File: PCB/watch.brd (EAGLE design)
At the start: 81.1 x 53.1 mm, 58 parts, among them IC1 ISL1209, J2 USB-MICROB, Q1 32.768 KHz, T1 BC850, U2 MKL27Z256VLH4

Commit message: wired more of the SR
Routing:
- net PTB18: track 0.00 -> 54.9 mm, vias 0 -> 1
- net PTC0: track 0.00 -> 47.3 mm, vias 0 -> 1
- net N$28: track 0.00 -> 47.1 mm
- net PTC7: track 0.00 -> 42.4 mm, vias 0 -> 1
- net PTB17: track 0.00 -> 35.7 mm, vias 0 -> 1
- net N$21: track 18.4 -> 26.9 mm, vias 1 -> 2
- net V+: track 0.00 -> 3.90 mm, vias 0 -> 2
- net GND: track 0.00 -> 2.75 mm, vias 0 -> 1
- net N$47: track 45.5 -> 44.9 mm

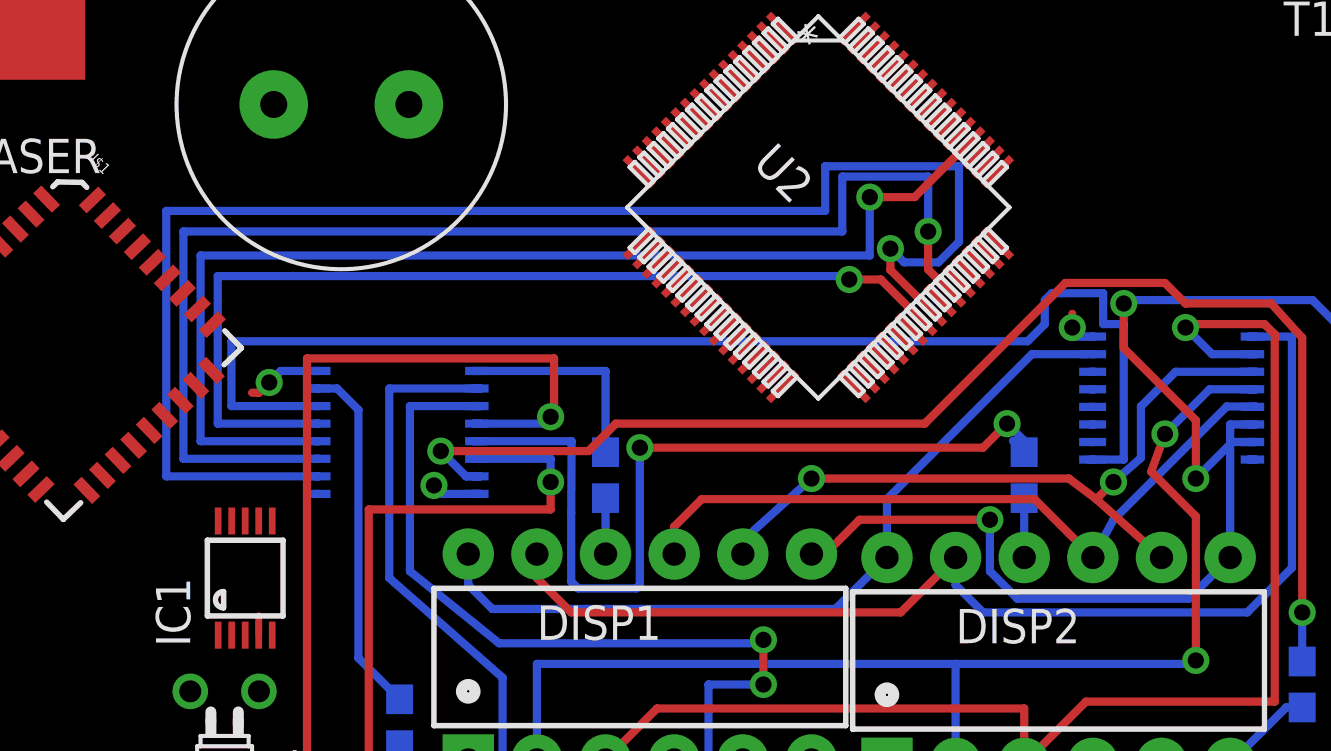
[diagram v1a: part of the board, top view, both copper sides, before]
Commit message: wired all SR but one pin
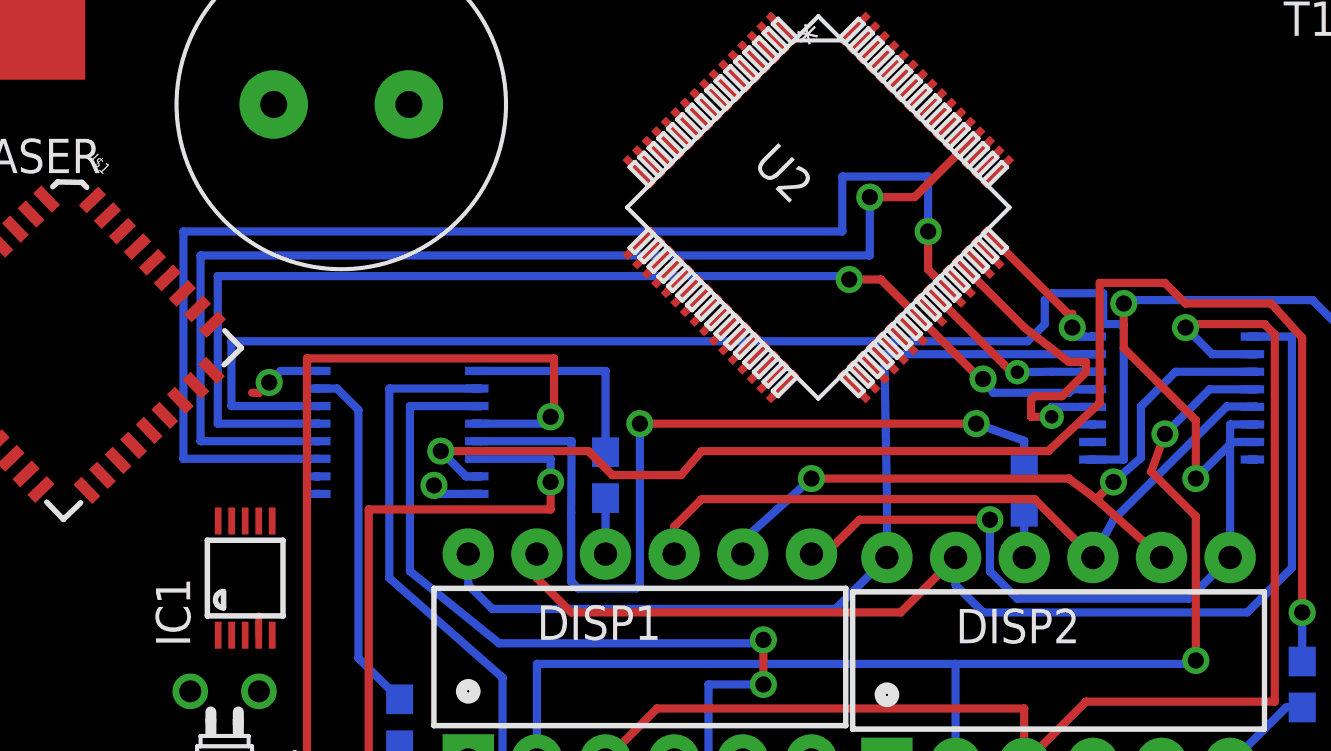
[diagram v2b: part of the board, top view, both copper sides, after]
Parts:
- moved R8 0.51 mm to (58.3, 31.5)
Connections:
- net PTB18: no longer U$4.MR, U$5.MR
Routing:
- net PTB18: track 54.9 -> 0.00 mm, vias 1 -> 0
- net PTC2: track 0.00 -> 11.5 mm, vias 0 -> 1
- net PTB17: track 35.7 -> 43.1 mm, vias 1 -> 2
- net PTB19: track 0.00 -> 6.54 mm, vias 0 -> 1
- net V+: track 3.90 -> 7.75 mm
- net N$29: track 49.2 -> 52.5 mm
- net N$11: track 29.6 -> 32.8 mm
- net N$15: track 2.20 -> 1.69 mm
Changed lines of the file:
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@@
 <element name="R6" library="SparkFun-Resistors" package="0603-RES" value="680" x="42.545" y="19.177" rot="MR0"/>
 <element name="R7" library="SparkFun-Resistors" package="0603-RES" value="680" x="51.689" y="19.304" rot="MR0"/>
-<element name="R8" library="SparkFun-Resistors" package="0603-RES" value="680" x="58.293" y="32.004" rot="MR90"/>
+<element name="R8" library="SparkFun-Resistors" package="0603-RES" value="680" x="58.293" y="31.496" rot="MR90"/>
 <element name="R9" library="SparkFun-Resistors" package="0603-RES" value="680" x="60.198" y="18.669" rot="MR0"/>
 <element name="S1" library="adafruit" package="EG1213" value="EG1213" x="79.248" y="57.785" rot="R180"/>
@@
 <via x="60.071" y="37.465" extent="1-16" drill="0.6" shape="square"/>
 <wire x1="60.071" y1="37.465" x2="60.071" y2="37.973" width="0.3048" layer="1"/>
+<wire x1="60.071" y1="37.973" x2="59.91330625" y2="37.973" width="0.3048" layer="1"/>
+<wire x1="59.91330625" y1="37.973" x2="57.302134375" y2="40.584171875" width="0.3048" layer="1"/>
 <wire x1="60.628" y1="37.129" x2="72.51" y2="40.35" width="0" layer="19" extent="1-16"/>
-<wire x1="57.302134375" y1="40.584171875" x2="60.071" y2="37.973" width="0" layer="19" extent="1-1"/>
 <wire x1="48.640065625" y1="35.98796875" x2="57.302134375" y2="40.584171875" width="0" layer="19" extent="1-1"/>
 <wire x1="45.104521875" y1="44.29648125" x2="48.640065625" y2="35.98796875" width="0" layer="19" extent="1-1"/>
@@
 <contactref element="U$5" pad="Q5"/>
 <contactref element="R8" pad="2"/>
-<wire x1="58.293" y1="32.854" x2="57.873" y2="33.274" width="0.3048" layer="16"/>
-<wire x1="44.069" y1="33.02" x2="44.069" y2="27.94" width="0.3048" layer="16"/>
+<wire x1="44.069" y1="33.909" x2="44.069" y2="27.94" width="0.3048" layer="16"/>
 <wire x1="44.069" y1="27.94" x2="43.942" y2="27.813" width="0.3048" layer="16"/>
 <wire x1="43.942" y1="27.813" x2="41.783" y2="27.813" width="0.3048" layer="16"/>
@@
 <wire x1="41.529" y1="30.607" x2="41.544" y2="33.259" width="0.3048" layer="16"/>
 <wire x1="41.544" y1="33.259" x2="38.166" y2="33.259" width="0.3048" layer="16"/>
-<via x="44.069" y="33.02" extent="1-16" drill="0.6" shape="square"/>
-<wire x1="44.069" y1="33.02" x2="56.769" y2="33.02" width="0.3048" layer="1"/>
-<wire x1="56.769" y1="33.02" x2="57.658" y2="33.909" width="0.3048" layer="1"/>
-<via x="57.658" y="33.909" extent="1-16" drill="0.6" shape="square"/>
-<wire x1="57.658" y1="33.909" x2="58.293" y2="33.274" width="0.3048" layer="16"/>
-<wire x1="58.293" y1="33.274" x2="58.293" y2="32.854" width="0.3048" layer="16"/>
+<via x="44.069" y="33.909" extent="1-16" drill="0.6" shape="square"/>
+<wire x1="44.069" y1="33.909" x2="56.515" y2="33.909" width="0.3048" layer="1"/>
+<via x="56.515" y="33.909" extent="1-16" drill="0.6" shape="square"/>
+<wire x1="56.515" y1="33.909" x2="58.293" y2="33.274" width="0.3048" layer="16"/>
+<wire x1="58.293" y1="33.274" x2="58.293" y2="32.346" width="0.3048" layer="16"/>
 </signal>
 <signal name="N$23">
@@
 <via x="36.703" y="32.893" extent="1-16" drill="0.6"/>
 <wire x1="36.703" y1="32.893" x2="42.164" y2="32.893" width="0.3048" layer="1"/>
-<wire x1="42.164" y1="32.893" x2="43.18" y2="33.909" width="0.3048" layer="1"/>
-<wire x1="54.61" y1="33.909" x2="59.817" y2="39.116" width="0.3048" layer="1"/>
-<wire x1="59.817" y1="39.116" x2="63.5" y2="39.116" width="0.3048" layer="1"/>
 <wire x1="63.5" y1="39.116" x2="64.262" y2="38.354" width="0.3048" layer="1"/>
 <wire x1="64.262" y1="38.354" x2="67.437" y2="38.354" width="0.3048" layer="1"/>
@@
 <via x="68.58" y="26.924" extent="1-16" drill="0.6"/>
 <wire x1="68.58" y1="26.924" x2="68.58" y2="25.107" width="0.3048" layer="16"/>
-<wire x1="43.18" y1="33.909" x2="54.61" y2="33.909" width="0.3048" layer="1"/>
+<wire x1="63.5" y1="39.116" x2="61.087" y2="39.116" width="0.3048" layer="1"/>
+<wire x1="61.087" y1="39.116" x2="61.087" y2="34.671" width="0.3048" layer="1"/>
+<wire x1="61.087" y1="34.671" x2="59.182" y2="32.893" width="0.3048" layer="1"/>
+<wire x1="59.182" y1="32.893" x2="46.355" y2="32.893" width="0.3048" layer="1"/>
+<wire x1="46.355" y1="32.893" x2="45.593" y2="32.004" width="0.3048" layer="1"/>
+<wire x1="45.593" y1="32.004" x2="43.053" y2="32.004" width="0.3048" layer="1"/>
+<wire x1="43.053" y1="32.004" x2="42.164" y2="32.893" width="0.3048" layer="1"/>
 </signal>
 <signal name="N$31">
@@
 <wire x1="51.816" y1="39.243" x2="52.986459375" y2="39.243" width="0.3048" layer="1"/>
 <wire x1="52.986459375" y1="39.243" x2="54.473709375" y2="37.75575" width="0.3048" layer="1"/>
-<wire x1="54.473709375" y1="37.75575" x2="60.628" y2="35.179" width="0" layer="19" extent="1-16"/>
+<wire x1="57.15" y1="35.052" x2="56.769" y2="35.56" width="0.3048" layer="16"/>
+<via x="56.769" y="35.56" extent="1-16" drill="0.6" shape="square"/>
+<wire x1="56.769" y1="35.56" x2="56.669459375" y2="35.56" width="0.3048" layer="1"/>
+<wire x1="56.669459375" y1="35.56" x2="54.473709375" y2="37.75575" width="0.3048" layer="1"/>
+<wire x1="57.15" y1="35.052" x2="59.944" y2="35.052" width="0.3048" layer="16"/>
+<wire x1="59.944" y1="35.052" x2="60.071" y2="35.179" width="0.3048" layer="16"/>
+<wire x1="60.071" y1="35.179" x2="60.628" y2="35.179" width="0.3048" layer="16"/>
 </signal>
 <signal name="PTB18">
-<contactref element="U$5" pad="MR"/>
-<contactref element="U$4" pad="MR"/>
 <contactref element="U2" pad="41"/>
-<wire x1="31.926" y1="31.959" x2="26.543" y2="31.959" width="0.3048" layer="16"/>
-<wire x1="26.543" y1="31.959" x2="26.543" y2="41.783" width="0.3048" layer="16"/>
-<wire x1="26.543" y1="41.783" x2="50.927" y2="41.783" width="0.3048" layer="16"/>
-<wire x1="50.927" y1="41.783" x2="50.927" y2="43.434" width="0.3048" layer="16"/>
-<wire x1="50.927" y1="43.434" x2="55.88" y2="43.434" width="0.3048" layer="16"/>
-<wire x1="55.88" y1="43.434" x2="55.88" y2="40.64" width="0.3048" layer="16"/>
-<wire x1="55.88" y1="40.64" x2="55.118" y2="39.878" width="0.3048" layer="16"/>
-<wire x1="55.118" y1="39.878" x2="53.848" y2="39.878" width="0.3048" layer="16"/>
-<wire x1="53.848" y1="39.878" x2="53.34" y2="40.386" width="0.3048" layer="16"/>
-<via x="53.34" y="40.386" extent="1-16" drill="0.6" shape="square"/>
-<wire x1="53.34" y1="40.386" x2="53.34" y2="39.596534375" width="0.3048" layer="1"/>
-<wire x1="53.34" y1="39.596534375" x2="54.827246875" y2="38.1092875" width="0.3048" layer="1"/>
-<wire x1="54.827246875" y1="38.1092875" x2="60.628" y2="33.229" width="0" layer="19" extent="1-16"/>
 </signal>
 <signal name="PTB19">
 <contactref element="U$4" pad="DS"/>
 <contactref element="U2" pad="42"/>
-<wire x1="55.18081875" y1="38.46285625" x2="60.628" y2="35.829" width="0" layer="19" extent="1-16"/>
+<wire x1="60.628" y1="35.829" x2="59.324" y2="35.829" width="0.3048" layer="16"/>
+<wire x1="59.324" y1="35.829" x2="58.039" y2="35.814" width="0.3048" layer="16"/>
+<via x="58.039" y="35.814" extent="1-16" drill="0.5"/>
+<wire x1="58.039" y1="35.814" x2="57.829675" y2="35.814" width="0.3048" layer="1"/>
+<wire x1="57.829675" y1="35.814" x2="55.18081875" y2="38.46285625" width="0.3048" layer="1"/>
 </signal>
 <signal name="PTB1">
@@
 <contactref element="U2" pad="45"/>
 <contactref element="U$4" pad="STCP"/>
-<wire x1="60.628" y1="34.529" x2="56.241475" y2="39.523515625" width="0" layer="19" extent="1-16"/>
+<wire x1="60.628" y1="34.529" x2="59.309" y2="34.529" width="0.3048" layer="16"/>
+<wire x1="59.309" y1="34.529" x2="59.309" y2="34.163" width="0.3048" layer="16"/>
+<via x="59.309" y="34.163" extent="1-16" drill="0.5"/>
+<wire x1="59.309" y1="34.163" x2="58.547" y2="34.163" width="0.3048" layer="1"/>
+<wire x1="58.547" y1="34.163" x2="58.547" y2="34.798" width="0.3048" layer="1"/>
+<wire x1="58.547" y1="34.798" x2="58.674" y2="34.925" width="0.3048" layer="1"/>
+<wire x1="58.674" y1="34.925" x2="59.69" y2="34.925" width="0.3048" layer="1"/>
+<wire x1="59.69" y1="34.925" x2="60.579" y2="35.814" width="0.3048" layer="1"/>
+<wire x1="60.579" y1="35.814" x2="60.579" y2="36.195" width="0.3048" layer="1"/>
+<wire x1="60.579" y1="36.195" x2="59.944" y2="36.195" width="0.3048" layer="1"/>
+<wire x1="58.299990625" y1="37.465" x2="56.241475" y2="39.523515625" width="0.3048" layer="1"/>
+<wire x1="58.299990625" y1="37.465" x2="59.944" y2="36.195" width="0.3048" layer="1"/>
 </signal>
 <signal name="N$19">
@@
 <wire x1="38.608" y1="27.051" x2="51.308" y2="27.051" width="0.3048" layer="16"/>
 <wire x1="51.308" y1="27.051" x2="53.213" y2="28.956" width="0.3048" layer="16"/>
-<wire x1="60.628" y1="36.479" x2="58.577" y2="36.479" width="0.3048" layer="16"/>
-<wire x1="58.577" y1="36.479" x2="53.213" y2="31.115" width="0.3048" layer="16"/>
+<wire x1="60.628" y1="36.479" x2="53.116" y2="36.479" width="0.3048" layer="16"/>
+<wire x1="53.116" y1="36.479" x2="53.213" y2="31.115" width="0.3048" layer="16"/>
 <wire x1="53.213" y1="31.115" x2="53.213" y2="28.956" width="0.3048" layer="16"/>
 </signal>
@@
 <contactref element="R8" pad="1"/>
 <contactref element="DISP2" pad="10"/>
-<wire x1="58.293" y1="31.154" x2="58.293" y2="28.956" width="0.3048" layer="16"/>
+<wire x1="58.293" y1="30.646" x2="58.293" y2="28.956" width="0.3048" layer="16"/>
 </signal>
 <signal name="N$20">

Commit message: w00t! wired all SR
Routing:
- net PTC0: track 47.3 -> 57.5 mm, vias 1 -> 2
- net PTC2: track 11.5 -> 10.7 mm
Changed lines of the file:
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@@
 <wire x1="54.737" y1="41.021" x2="54.737" y2="39.613778125" width="0.3048" layer="1"/>
 <wire x1="54.737" y1="39.613778125" x2="55.53436875" y2="38.816409375" width="0.3048" layer="1"/>
-<wire x1="55.53436875" y1="38.816409375" x2="60.628" y2="33.879" width="0" layer="19" extent="1-16"/>
+<wire x1="55.53436875" y1="38.816409375" x2="57.774778125" y2="36.576" width="0.3048" layer="1"/>
+<wire x1="57.774778125" y1="36.576" x2="58.42" y2="36.576" width="0.3048" layer="1"/>
+<wire x1="58.42" y1="36.576" x2="58.928" y2="36.068" width="0.3048" layer="1"/>
+<wire x1="58.928" y1="36.068" x2="58.928" y2="35.56" width="0.3048" layer="1"/>
+<wire x1="58.928" y1="35.56" x2="57.785" y2="34.29" width="0.3048" layer="1"/>
+<via x="57.785" y="34.29" extent="1-16" drill="0.6"/>
+<wire x1="57.785" y1="34.29" x2="58.928" y2="33.401" width="0.3048" layer="16"/>
+<wire x1="58.928" y1="33.401" x2="59.817" y2="33.401" width="0.3048" layer="16"/>
+<wire x1="59.817" y1="33.401" x2="60.168" y2="33.879" width="0.3048" layer="16"/>
+<wire x1="60.168" y1="33.879" x2="60.628" y2="33.879" width="0.3048" layer="16"/>
 </signal>
 <signal name="PTC2">
 <contactref element="U2" pad="45"/>
 <contactref element="U$4" pad="STCP"/>
-<wire x1="60.628" y1="34.529" x2="59.309" y2="34.529" width="0.3048" layer="16"/>
-<wire x1="59.309" y1="34.529" x2="59.309" y2="34.163" width="0.3048" layer="16"/>
-<via x="59.309" y="34.163" extent="1-16" drill="0.5"/>
-<wire x1="59.309" y1="34.163" x2="58.547" y2="34.163" width="0.3048" layer="1"/>
-<wire x1="58.547" y1="34.163" x2="58.547" y2="34.798" width="0.3048" layer="1"/>
-<wire x1="58.547" y1="34.798" x2="58.674" y2="34.925" width="0.3048" layer="1"/>
-<wire x1="58.674" y1="34.925" x2="59.69" y2="34.925" width="0.3048" layer="1"/>
+<wire x1="60.628" y1="34.529" x2="60.071" y2="34.529" width="0.3048" layer="16"/>
+<wire x1="60.071" y1="34.529" x2="59.436" y2="34.163" width="0.3048" layer="16"/>
+<via x="59.436" y="34.163" extent="1-16" drill="0.5"/>
+<wire x1="59.436" y1="34.163" x2="58.801" y2="34.163" width="0.3048" layer="1"/>
+<wire x1="58.801" y1="34.671" x2="58.928" y2="34.925" width="0.3048" layer="1"/>
+<wire x1="58.928" y1="34.925" x2="59.69" y2="34.925" width="0.3048" layer="1"/>
 <wire x1="59.69" y1="34.925" x2="60.579" y2="35.814" width="0.3048" layer="1"/>
 <wire x1="60.579" y1="35.814" x2="60.579" y2="36.195" width="0.3048" layer="1"/>
@@
 <wire x1="58.299990625" y1="37.465" x2="56.241475" y2="39.523515625" width="0.3048" layer="1"/>
 <wire x1="58.299990625" y1="37.465" x2="59.944" y2="36.195" width="0.3048" layer="1"/>
+<wire x1="58.801" y1="34.671" x2="58.801" y2="34.163" width="0.3048" layer="1"/>
 </signal>
 <signal name="N$19">

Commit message: cleaned up crap
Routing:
- net PTC2: track 10.7 -> 7.97 mm
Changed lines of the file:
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@@
 <wire x1="60.116" y1="37.129" x2="60.071" y2="37.465" width="0.3048" layer="16"/>
 <via x="60.071" y="37.465" extent="1-16" drill="0.6" shape="square"/>
-<wire x1="60.071" y1="37.465" x2="60.071" y2="37.973" width="0.3048" layer="1"/>
-<wire x1="60.071" y1="37.973" x2="59.91330625" y2="37.973" width="0.3048" layer="1"/>
-<wire x1="59.91330625" y1="37.973" x2="57.302134375" y2="40.584171875" width="0.3048" layer="1"/>
+<wire x1="60.071" y1="37.81530625" x2="57.302134375" y2="40.584171875" width="0.3048" layer="1"/>
+<wire x1="60.071" y1="37.81530625" x2="60.071" y2="37.465" width="0.3048" layer="1"/>
+<wire x1="72.51" y1="40.35" x2="81.248" y2="57.785" width="0" layer="19" extent="1-1"/>
 <wire x1="60.628" y1="37.129" x2="72.51" y2="40.35" width="0" layer="19" extent="1-16"/>
 <wire x1="48.640065625" y1="35.98796875" x2="57.302134375" y2="40.584171875" width="0" layer="19" extent="1-1"/>
@@
 <wire x1="20.32" y1="48.26" x2="20.9619125" y2="41.109865625" width="0" layer="19" extent="1-1"/>
 <wire x1="13.274" y1="42.715" x2="20.9619125" y2="41.109865625" width="0" layer="19" extent="1-1"/>
-<wire x1="81.248" y1="57.785" x2="72.51" y2="40.35" width="0" layer="19" extent="1-1"/>
 <wire x1="-14.39" y1="69.85" x2="13.274" y2="42.715" width="0" layer="19" extent="1-1"/>
 <wire x1="-23.71" y1="73.66" x2="-14.39" y2="69.85" width="0" layer="19" extent="1-1"/>
@@
 <wire x1="60.071" y1="34.529" x2="59.436" y2="34.163" width="0.3048" layer="16"/>
 <via x="59.436" y="34.163" extent="1-16" drill="0.5"/>
-<wire x1="59.436" y1="34.163" x2="58.801" y2="34.163" width="0.3048" layer="1"/>
-<wire x1="58.801" y1="34.671" x2="58.928" y2="34.925" width="0.3048" layer="1"/>
-<wire x1="58.928" y1="34.925" x2="59.69" y2="34.925" width="0.3048" layer="1"/>
-<wire x1="59.69" y1="34.925" x2="60.579" y2="35.814" width="0.3048" layer="1"/>
-<wire x1="60.579" y1="35.814" x2="60.579" y2="36.195" width="0.3048" layer="1"/>
-<wire x1="60.579" y1="36.195" x2="59.944" y2="36.195" width="0.3048" layer="1"/>
-<wire x1="58.299990625" y1="37.465" x2="56.241475" y2="39.523515625" width="0.3048" layer="1"/>
-<wire x1="58.299990625" y1="37.465" x2="59.944" y2="36.195" width="0.3048" layer="1"/>
-<wire x1="58.801" y1="34.671" x2="58.801" y2="34.163" width="0.3048" layer="1"/>
+<wire x1="59.436" y1="34.163" x2="58.801" y2="34.163" width="0" layer="19" extent="1-16"/>
+<wire x1="59.436" y1="36.328990625" x2="56.241475" y2="39.523515625" width="0.3048" layer="1"/>
+<wire x1="59.436" y1="36.328990625" x2="59.436" y2="34.163" width="0.3048" layer="1"/>
 </signal>
 <signal name="N$19">
